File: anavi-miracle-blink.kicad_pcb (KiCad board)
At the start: 2 copper layers, 46.5 x 32.8 mm, 16 parts, among them J4 Conn_01x04_Female, J7 Screw_Terminal_01x03, U1 MOUDLE-SEEEDUINO-XIAO-ESP32C3, U2 74LVC1G17W5-7

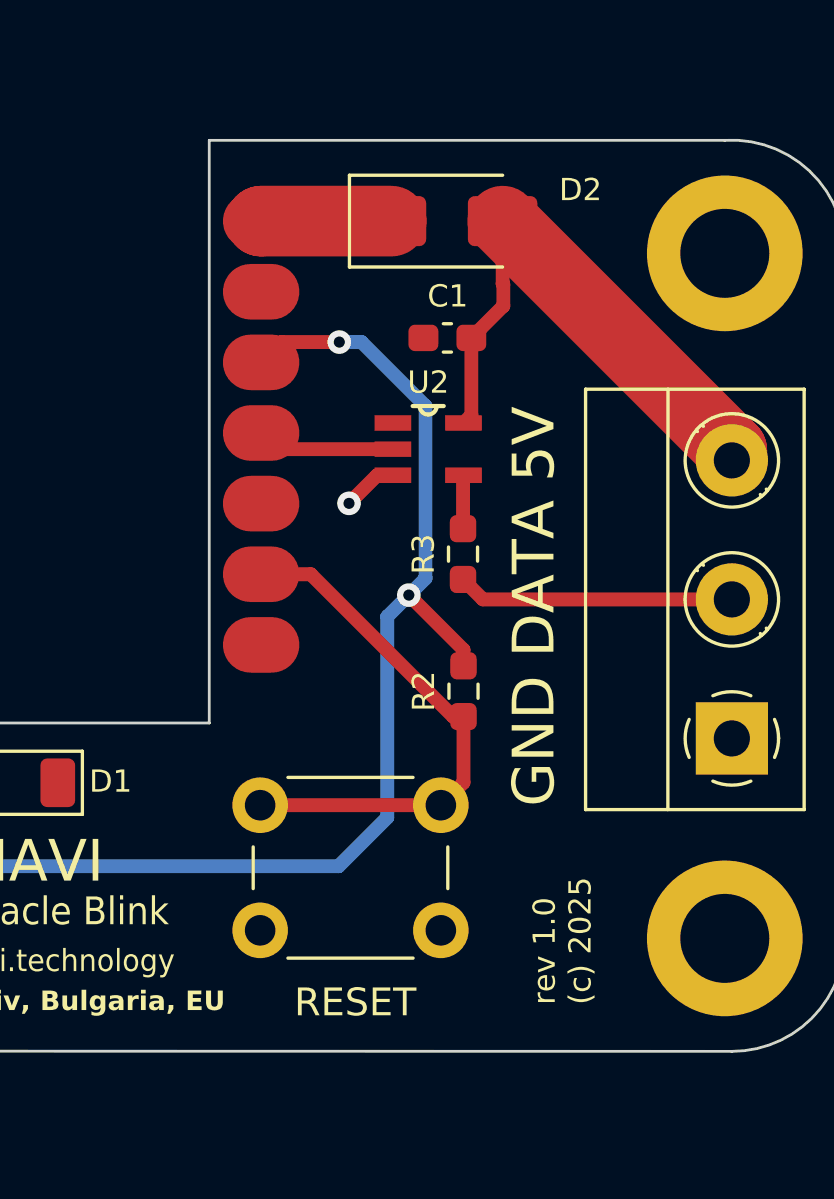
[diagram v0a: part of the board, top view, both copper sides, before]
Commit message: Rev 1.1: Remove Schottky diode
Remove Schottky diode to allow using the USB-C as power source for
NeoPixel LEDs. The Schottky diode can still be added externally in
the use case of external 5V power supply.

Signed-off-by: Leon Anavi <leon@anavi.org>
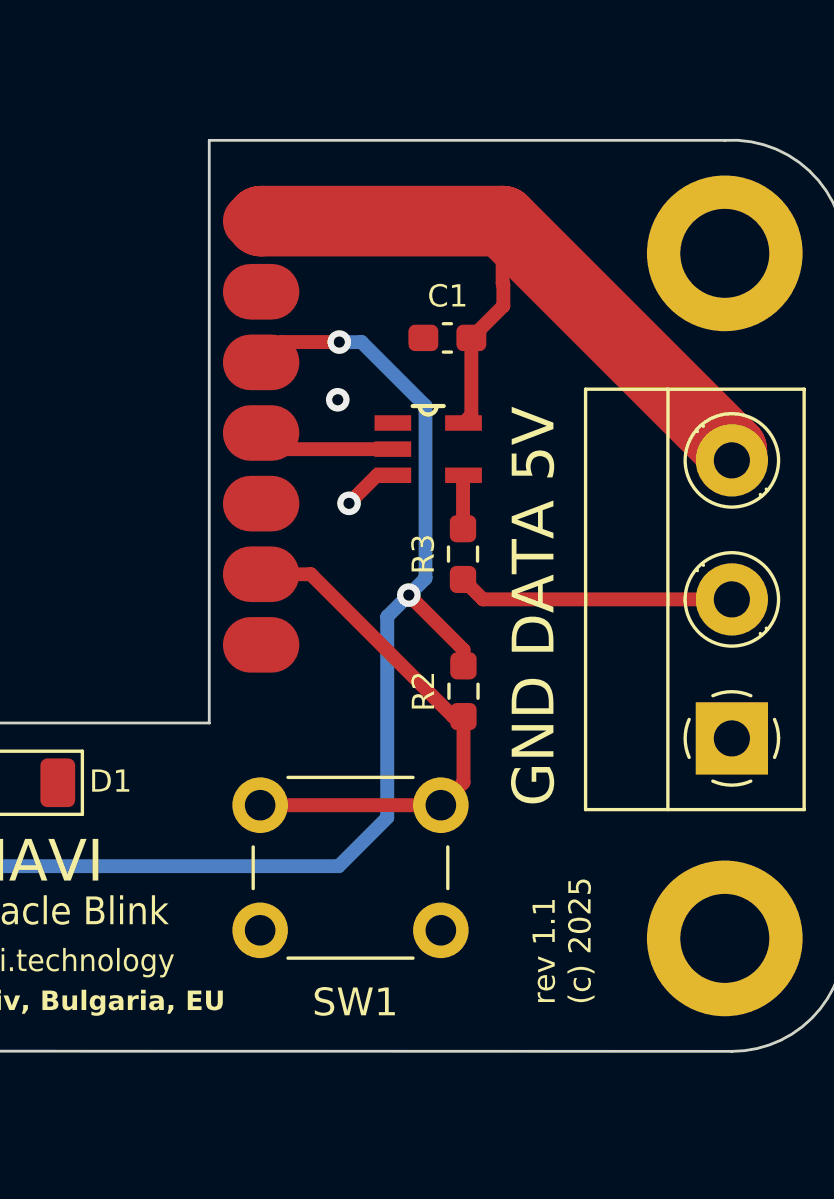
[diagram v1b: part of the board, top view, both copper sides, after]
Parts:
- removed D2: D_Schottky, Diode_SMD:D_SMA
- renumbered RESET to SW1
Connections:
- U1 pad 14: Net-(D2-K) -> +5V
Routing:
- net +5V: track 19.9 -> 28.6 mm
- net Net-(D2-K): track 4.69 -> 0.00 mm
- net GND: vias 1 -> 2
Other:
- board text added: "rev 1.1 (c) 2025"
- board text removed: "rev 1.0 (c) 2025"
